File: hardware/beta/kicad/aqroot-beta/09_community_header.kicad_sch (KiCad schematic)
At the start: 16 parts, among them J5 COMMUNITY_HEADER_2x13, U15 TPS22918, U16 TCA9517ADGK

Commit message: AQROOT Beta: fix accessory rail naming and I2C grounding
Three contained fixes in 09_COMMUNITY_HEADER. Verified with scratch kicad-cli
netlist and ERC comparison against ec0a428.

- Restores the ACC_3V3_SW net name. The empty label at (273.05, 99.06) that
  KiCad was resolving in preference to ACC_3V3_SW is removed, and the rail
  label is re-placed at (274.32, 99.06). The rail now exports as
  /09_COMMUNITY_HEADER/ACC_3V3_SW with the expected 9 nodes: U15.6, U16.8,
  C38.1, C42.2, R46.2, R49.2, R50.2, TP12.1 and J5.26. No <NO NET> rail and no
  multiple_net_names violation remain.
- Grounds the TCA9517A directly. U16 pin 4 now joins the board GND net via a
  wire from (218.44, 90.17) to a GND symbol at (218.44, 91.44).
- Removes the erroneous series ground capacitor C41, which had left U16 pin 4
  DC-isolated on the two-node net Net-(U16-GND) = {U16.4, C41.2}. That net no
  longer exists. C40 remains +3V3/VCCA to GND and C42 remains ACC_3V3_SW/VCCB
  to GND.
- Marks the external I2C pull-ups DNP. R49 and R50 now carry the actual KiCad
  (dnp yes) property rather than only the word DNP in their Value strings.
  Values remain 4.7k, R49 between ACC_3V3_SW and I2C_SDA_EXT_HDR, R50 between
  ACC_3V3_SW and I2C_SCL_EXT_HDR.

No new functional blocks. A full net-membership comparison shows exactly four
nets changed, all intended: <NO NET> removed, ACC_3V3_SW added, GND gained
U16.4 and lost C41.1, Net-(U16-GND) removed. Every other net is byte-identical,
so the XGPIO, WAKE, FAST_IO and RootProbe sections are untouched.

ERC total 250 -> 248: multiple_net_names 1 -> 0 and power_pin_not_driven
6 -> 5. No new violation categories.

Still not fabrication-ready: footprints are unassigned on C37-C42, R46-R50 and
TP12, and the XGPIO, WAKE and FAST_IO protection blocks remain incomplete.

Co-Authored-By: Claude Opus 5 <noreply@anthropic.com>
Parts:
- removed C41: 100 nF X7R, symbol Device:C
- R49, R50: now not fitted
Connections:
- net GND: now also U16.4 (GND)
- net ACC_3V3_SW: now reaches C38.1, C42.2, J5.26 (Pin_26), R46.2, R49.2, R50.2, TP12.1, U15.6 (VOUT), U16.8 (VCCB)
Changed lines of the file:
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@@
 	(wire
 		(pts
-			(xy 214.63 97.79) (xy 218.44 97.79)
-		)
-		(stroke
-			(width 0)
-			(type default)
-		)
-	)
-	(wire
-		(pts
-			(xy 218.44 90.17) (xy 218.44 97.79)
-		)
-		(stroke
-			(width 0)
-			(type default)
-		)
-	)
-	(wire
-		(pts
 			(xy 180.34 134.62) (xy 180.34 135.89)
 		)
@@
 	(wire
 		(pts
+			(xy 218.44 90.17) (xy 218.44 91.44)
+		)
+		(stroke
+			(width 0)
+			(type default)
+		)
+	)
+	(wire
+		(pts
 			(xy 266.7 82.55) (xy 266.7 85.09)
 		)
@@
 	(wire
 		(pts
-			(xy 205.74 97.79) (xy 207.01 97.79)
-		)
-		(stroke
-			(width 0)
-			(type default)
-		)
-	)
-	(wire
-		(pts
 			(xy 265.43 109.22) (xy 266.7 109.22)
 		)
@@
 	(wire
 		(pts
-			(xy 273.05 99.06) (xy 275.59 99.06)
+			(xy 283.21 88.9) (xy 283.21 99.06)
 		)
 		(stroke
@@
 	(wire
 		(pts
-			(xy 283.21 88.9) (xy 283.21 99.06)
+			(xy 260.35 59.69) (xy 260.35 72.39)
 		)
 		(stroke
@@
 	(wire
 		(pts
-			(xy 260.35 59.69) (xy 260.35 72.39)
+			(xy 182.88 154.94) (xy 184.15 154.94)
 		)
 		(stroke
@@
 	(wire
 		(pts
-			(xy 182.88 154.94) (xy 184.15 154.94)
+			(xy 265.43 116.84) (xy 266.7 116.84)
 		)
 		(stroke
@@
 	(wire
 		(pts
-			(xy 265.43 116.84) (xy 266.7 116.84)
+			(xy 232.41 74.93) (xy 231.14 74.93)
 		)
 		(stroke
@@
 	(wire
 		(pts
-			(xy 232.41 74.93) (xy 231.14 74.93)
+			(xy 265.43 114.3) (xy 266.7 114.3)
 		)
 		(stroke
@@
 	(wire
 		(pts
-			(xy 265.43 114.3) (xy 266.7 114.3)
+			(xy 200.66 59.69) (xy 201.93 59.69)
 		)
 		(stroke
@@
 	(wire
 		(pts
-			(xy 200.66 59.69) (xy 201.93 59.69)
+			(xy 274.32 99.06) (xy 275.59 99.06)
 		)
 		(stroke
@@
 		)
 	)
+	(label "ACC_3V3_SW"
+		(at 274.32 99.06 180)
+		(effects
+			(font
+				(size 1.27 1.27)
+			)
+			(justify right bottom)
+		)
+	)
 	(label "ACC_PWR_EN"
 		(at 184.15 143.51 180)
@@
 		)
 	)
-	(label ""
-		(at 273.05 99.06 0)
-		(effects
-			(font
-				(size 1.27 1.27)
-			)
-			(justify left bottom)
-		)
-	)
 	(label "FAST_IO_GPIO43_HDR"
 		(at 251.46 137.16 180)
@@
 		)
 	)
-	(label "ACC_3V3_SW"
-		(at 275.59 99.06 180)
-		(effects
-			(font
-				(size 1.27 1.27)
-			)
-			(justify right bottom)
-		)
-	)
 	(hierarchical_label "XGPIO6"
 		(shape bidirectional)
@@
 		(on_board yes)
 		(in_pos_files yes)
-		(dnp no)
+		(dnp yes)
 		(property "Reference" "R50"
 			(at 278.638 93.472 90)
@@
 		(on_board yes)
 		(in_pos_files yes)
-		(dnp no)
+		(dnp yes)
 		(property "Reference" "R49"
 			(at 240.284 94.996 90)
@@
 	(symbol
 		(lib_id "power:GND")
-		(at 205.74 97.79 270)
+		(at 218.44 91.44 0)
 		(unit 1)
 		(body_style 1)
@@
 		(in_pos_files yes)
 		(dnp no)
-		(fields_autoplaced yes)
 		(property "Reference" "#PWR0169"
-			(at 199.39 97.79 0)
+			(at 218.44 97.79 0)
 			(hide yes)
 			(show_name no)
@@
 		)
 		(property "Value" "GND"
-			(at 201.93 97.7899 90)
+			(at 213.868 91.694 0)
 			(show_name no)
 			(do_not_autoplace no)
@@
 					(size 1.27 1.27)
 				)
-				(justify right)
+				(justify left)
 			)
 		)
 		(property "Footprint" ""
-			(at 205.74 97.79 0)
+			(at 218.44 91.44 0)
 			(hide yes)
 			(show_name no)
@@
 		)
 		(property "Datasheet" ""
-			(at 205.74 97.79 0)
+			(at 218.44 91.44 0)
 			(hide yes)
 			(show_name no)
@@
 		)
 		(property "Description" "Power symbol creates a global label with name \"GND\" , ground"
-			(at 205.74 97.79 0)
+			(at 218.44 91.44 0)
 			(hide yes)
 			(show_name no)
@@
 					(unit 1)
 				)
-			)
-		)
-	)
-	(symbol
-		(lib_id "Device:C")
-		(at 210.82 97.79 90)
-		(unit 1)
-		(body_style 1)
-		(exclude_from_sim no)
-		(in_bom yes)
-		(on_board yes)
-		(in_pos_files yes)
-		(dnp no)
-		(fields_autoplaced yes)
-		(property "Reference" "C41"
-			(at 210.82 90.17 90)
-			(show_name no)
-			(do_not_autoplace no)
-			(effects
-				(font
-					(size 1.27 1.27)
-				)
-			)
-		)
-		(property "Value" "100 nF X7R"
-			(at 210.82 92.71 90)
-			(show_name no)
-			(do_not_autoplace no)
-			(effects
-				(font
-					(size 1.27 1.27)
-				)
-			)
-		)
-		(property "Footprint" ""
-			(at 214.63 96.8248 0)
-			(hide yes)
-			(show_name no)
-			(do_not_autoplace no)
-			(effects
-				(font
-					(size 1.27 1.27)
-				)
-			)
-		)
-		(property "Datasheet" ""
-			(at 210.82 97.79 0)
-			(hide yes)
-			(show_name no)
-			(do_not_autoplace no)
-			(effects
-				(font
-					(size 1.27 1.27)
-				)
-			)
-		)
-		(property "Description" "Unpolarized capacitor"
-			(at 210.82 97.79 0)
-			(hide yes)
-			(show_name no)
-			(do_not_autoplace no)
-			(effects
-				(font
-					(size 1.27 1.27)
-				)
-			)
-		)
-		(pin "1"
-		)
-		(pin "2"
-		)
-		(instances
-			(project "aqroot-Beta"
-				(path "/8a0ad1ee-a49e-4cff-9a78-44823e373405/fc294db1-6eef-4bd8-b4f0-c1bd635657ed"
-					(reference "C41")
-					(unit 1)
-				)

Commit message: AQROOT Beta: assign footprints to community-header passives
Assign footprints to the 11 previously unfootprinted parts on the
09_COMMUNITY_HEADER sheet. Sizes were derived from parts already in this
project rather than chosen independently.

- C37, C38 (1uF 10V X7R)        -> Capacitor_SMD:C_0603_1608Metric
- C39, C40, C42 (100nF X7R)     -> Capacitor_SMD:C_0603_1608Metric
- R46, R47, R48, R49, R50       -> Resistor_SMD:R_0603_1608Metric
- TP12                          -> TestPoint:TestPoint_Pad_D1.0mm

Basis for the sizes:
- C25 is exactly "1uF 10V X7R" on 0603, and C28 and C36 are "100nF X7R" on
  0603. The project reserves 0805 and 1206 for bulk capacitors of 4.7uF and
  above (C20, C26-C35), so both values map unambiguously to 0603.
- All 16 already-footprinted resistors in the project use R_0603_1608Metric
  with no exceptions.
- TP12 matches TP8-TP11. The library-qualified form is used deliberately;
  TP6 and TP7 carry a bare footprint name and are the source of the two
  existing footprint_link_issues ERC warnings, which are left untouched here.

Sheet 09 footprint coverage is now 15 of 15 parts. C41 is absent from this list
because it was removed as the erroneous series ground capacitor in b96a247.

Property changes only: 11 changed lines, every one a Footprint property that
was previously empty. No connectivity, symbol, value or geometry changes.
Verified with kicad-cli netlist export (exit 0) and an ERC comparison that is
unchanged at 248 violations with no new categories, as expected when only
footprint assignments change.

All three footprints verified present in the installed KiCad libraries with the
expected pad counts.

Co-Authored-By: Claude Opus 5 <noreply@anthropic.com>
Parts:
- C37, C38, C39, C40, C42: footprint (none) -> Capacitor_SMD:C_0603_1608Metric
- R46, R47, R48, R49, R50: footprint (none) -> Resistor_SMD:R_0603_1608Metric
- TP12: footprint (none) -> TestPoint:TestPoint_Pad_D1.0mm
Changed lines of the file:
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@@
 			)
 		)
-		(property "Footprint" ""
+		(property "Footprint" "Resistor_SMD:R_0603_1608Metric"
 			(at 237.49 71.628 90)
 			(hide yes)
@@
 			)
 		)
-		(property "Footprint" ""
+		(property "Footprint" "Resistor_SMD:R_0603_1608Metric"
 			(at 279.4 97.282 90)
 			(hide yes)
@@
 			)
 		)
-		(property "Footprint" ""
+		(property "Footprint" "Resistor_SMD:R_0603_1608Metric"
 			(at 205.232 157.48 90)
 			(hide yes)
@@
 			)
 		)
-		(property "Footprint" ""
+		(property "Footprint" "Capacitor_SMD:C_0603_1608Metric"
 			(at 209.55 58.7248 0)
 			(hide yes)
@@
 			)
 		)
-		(property "Footprint" ""
+		(property "Footprint" "Resistor_SMD:R_0603_1608Metric"
 			(at 240.03 102.108 90)
 			(hide yes)
@@
 			)
 		)
-		(property "Footprint" ""
+		(property "Footprint" "TestPoint:TestPoint_Pad_D1.0mm"
 			(at 219.71 130.81 0)
 			(hide yes)
@@
 			)
 		)
-		(property "Footprint" ""
+		(property "Footprint" "Capacitor_SMD:C_0603_1608Metric"
 			(at 215.5952 146.05 0)
 			(hide yes)
@@
 			)
 		)
-		(property "Footprint" ""
+		(property "Footprint" "Capacitor_SMD:C_0603_1608Metric"
 			(at 181.3052 134.62 0)
 			(hide yes)
@@
 			)
 		)
-		(property "Footprint" ""
+		(property "Footprint" "Resistor_SMD:R_0603_1608Metric"
 			(at 237.49 81.788 90)
 			(hide yes)
@@
 			)
 		)
-		(property "Footprint" ""
+		(property "Footprint" "Capacitor_SMD:C_0603_1608Metric"
 			(at 222.25 63.1952 0)
 			(hide yes)
@@
 			)
 		)
-		(property "Footprint" ""
+		(property "Footprint" "Capacitor_SMD:C_0603_1608Metric"
 			(at 191.77 153.9748 0)
 			(hide yes)

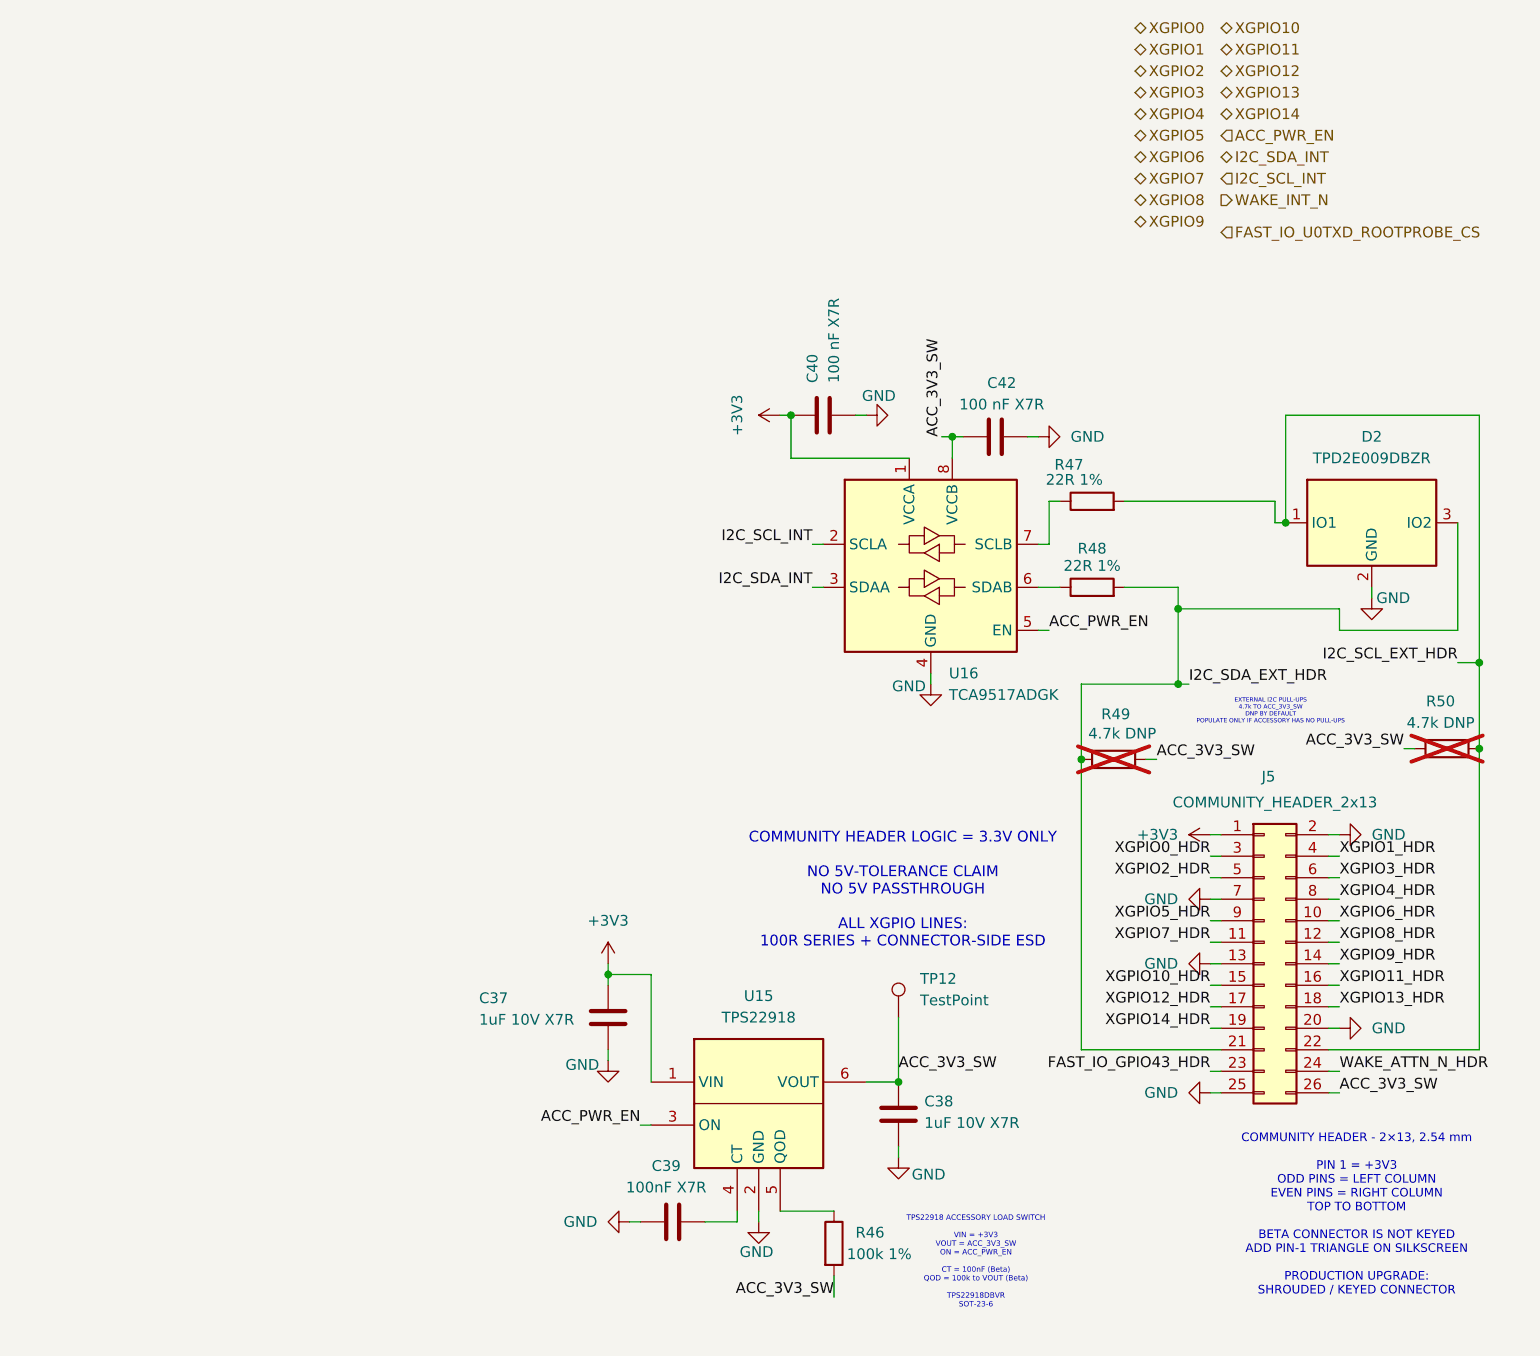
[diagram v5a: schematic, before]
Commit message: AQROOT Beta: add protected XGPIO community-header interface
Add the protected XGPIO interface on 09_COMMUNITY_HEADER: fifteen 100R series
resistors and four TPD4E1B06DRLR ESD arrays between the internal XGPIO nets and
the community header J5.

Topology, per line: internal /XGPIOx -> 100R series resistor -> XGPIOx_HDR ->
J5 pin, with the ESD channel tapped on the XGPIOx_HDR (connector) side of the
resistor. Every ESD channel is a leaf on its net, so no channel is wired in
series with the signal.

Channel mapping:
- D3: IO1 XGPIO0_HDR, IO2 XGPIO1_HDR, IO3 XGPIO2_HDR, IO4 XGPIO3_HDR
- D4: IO1 XGPIO4_HDR, IO2 XGPIO5_HDR, IO3 XGPIO6_HDR, IO4 XGPIO7_HDR
- D5: IO1 XGPIO8_HDR, IO2 XGPIO9_HDR, IO3 XGPIO10_HDR, IO4 XGPIO11_HDR
- D6: IO1 XGPIO12_HDR, IO2 XGPIO13_HDR, IO3 XGPIO14_HDR, IO4 unused

Verified with a scratch kicad-cli netlist export and ERC comparison against
4e1dcc4:
- All 15 XGPIOx_HDR nets (x=0..14) contain exactly three nodes: one J5 pin, one
  resistor pin and one ESD channel pin, with the header number matching the
  internal channel number.
- No XGPIO lines are shorted together. No XGPIO4_HDR..XGPIO14_HDR net is
  orphaned.
- Exactly 15 resistors R51-R65, all 100R 1%, all
  Resistor_SMD:R_0603_1608Metric. No stray R66+ and no XGPIO15 net.
- All four arrays are TPD4E1B06DRLR on Package_TO_SOT_SMD:SOT-563 with pin 2 on
  board GND.
- D6 IO4 (pin 6) and all four NC pins (pin 5) remain unwired.

An earlier iteration of this work had the header-side labels of the D4, D5 and
D6 blocks left at XGPIO0_HDR..XGPIO3_HDR after block replication, which shorted
the 15 GPIO lines into 4 groups and orphaned 11 header pins. Ten labels were
renumbered to correct it; that state was never committed.

ERC total 248 -> 234. label_dangling 56 -> 26. The +15 in isolated_pin_label is
the fifteen new internal /XGPIOx nets, which stay single-node until the MCU and
expander side is wired.

Known remaining work: WAKE protection, FAST_IO protection and the RootProbe
placeholder are all in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
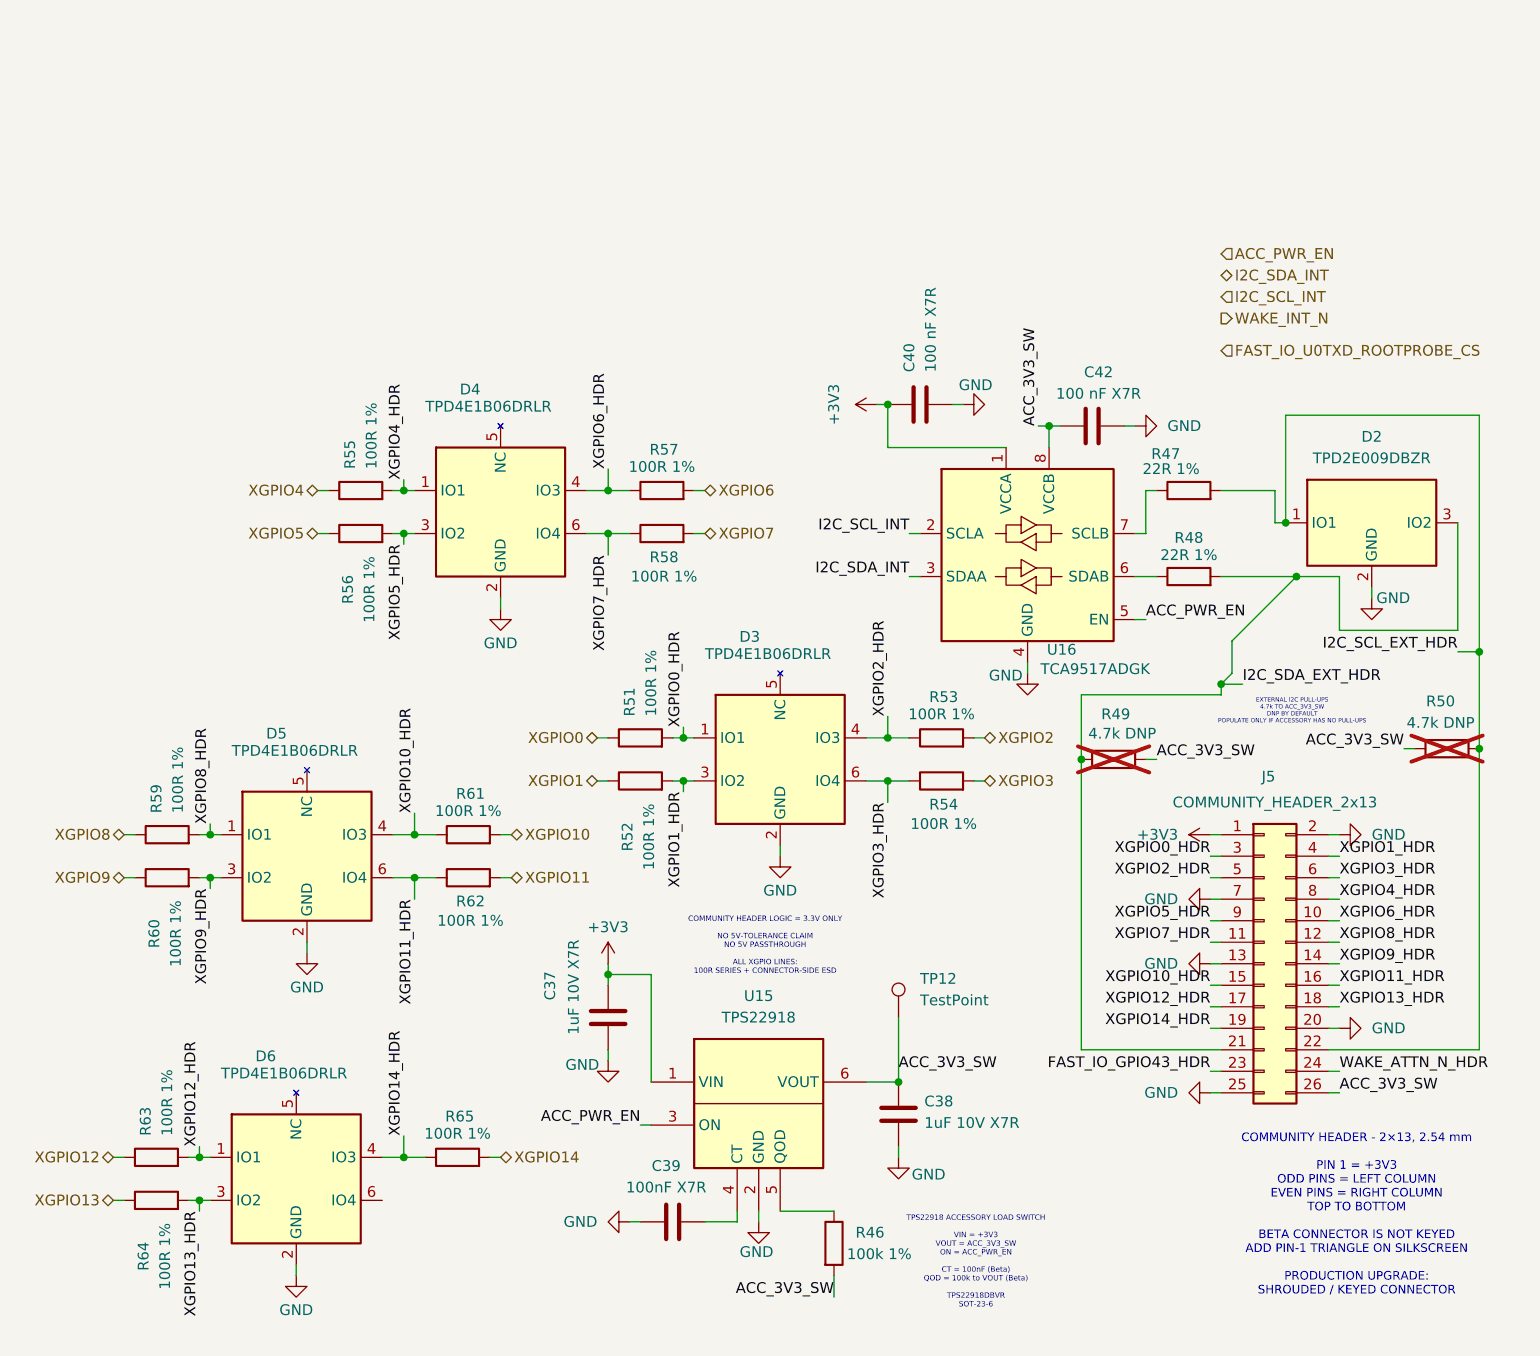
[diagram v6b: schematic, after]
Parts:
- added D3, D4, D5, D6: TPD4E1B06DRLR, Package_TO_SOT_SMD:SOT-563, symbol AQROOT_Beta:TPD4E1B06DRLR
- added R51, R52, R53, R54, R55, R56, R57, R58, R59, R60, R61, R62, R63, R64, R65: 100R 1%, Resistor_SMD:R_0603_1608Metric, symbol Device:R
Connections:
- net GND: now also D3.2 (GND), D4.2 (GND), D5.2 (GND), D6.2 (GND)
- net XGPIO0: now also R51.1
- net XGPIO0_HDR: now also D3.1 (IO1), R51.2
- net XGPIO1: now also R52.1
- net XGPIO10: now also R61.2
- net XGPIO10_HDR: now also D5.4 (IO3), R61.1
- net XGPIO11: now also R62.2
- net XGPIO11_HDR: now also D5.6 (IO4), R62.1
- net XGPIO12: now also R63.1
- net XGPIO12_HDR: now also D6.1 (IO1), R63.2
- net XGPIO13: now also R64.1
- net XGPIO13_HDR: now also D6.3 (IO2), R64.2
- net XGPIO14: now also R65.2
- net XGPIO14_HDR: now also D6.4 (IO3), R65.1
- net XGPIO1_HDR: now also D3.3 (IO2), R52.2
- net XGPIO2: now also R53.2
- net XGPIO2_HDR: now also D3.4 (IO3), R53.1
- net XGPIO3: now also R54.2
- net XGPIO3_HDR: now also D3.6 (IO4), R54.1
- net XGPIO4: now also R55.1
- net XGPIO4_HDR: now also D4.1 (IO1), R55.2
- net XGPIO5: now also R56.1
- net XGPIO5_HDR: now also D4.3 (IO2), R56.2
- net XGPIO6: now also R57.2
- net XGPIO6_HDR: now also D4.4 (IO3), R57.1
- net XGPIO7: now also R58.2
- net XGPIO7_HDR: now also D4.6 (IO4), R58.1
- net XGPIO8: now also R59.1
- net XGPIO8_HDR: now also D5.1 (IO1), R59.2
- net XGPIO9: now also R60.1
- net XGPIO9_HDR: now also D5.3 (IO2), R60.2
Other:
- moved on the sheet: C40, C42, R47, R48, U16
